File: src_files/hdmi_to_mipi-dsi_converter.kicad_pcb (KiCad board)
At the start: 4 copper layers, 90 x 55 mm, 145 parts, among them J1 HDMI-019S, J2 HDMI-019S, J3 Conn_02x05_Odd_Even, J4 USB_B_Micro, J5 XF2M60151AH, J6 Conn_01x02, J7 XF2M60151AH, U1 MCP1700-1202E_SOT23, U2 AX1007E18A, U3 ME6211A33PG-N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

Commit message: updated all files and production files as well
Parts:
- added R28: 0R, Resistor_SMD:R_0603_1608Metric, F.Cu at (165.6, 60.6)
- FB1, FB4: footprint Barrel - Audio Connectors:BEADC2012X105N -> Inductor_SMD:L_0603_1608Metric
- FB2: footprint Inductor_SMD:L_0805_2012Metric -> Inductor_SMD:L_0603_1608Metric
- FB3: footprint Resistor_SMD:R_0603_1608Metric -> Inductor_SMD:L_0603_1608Metric
- U8: footprint Barrel - Audio Connectors:QFN40P180X180X55-12N -> SamacSys_Parts_2:QFN40P180X180X55-12N
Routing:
- net GND: track 192.5 -> 191.7 mm, vias 118 -> 117

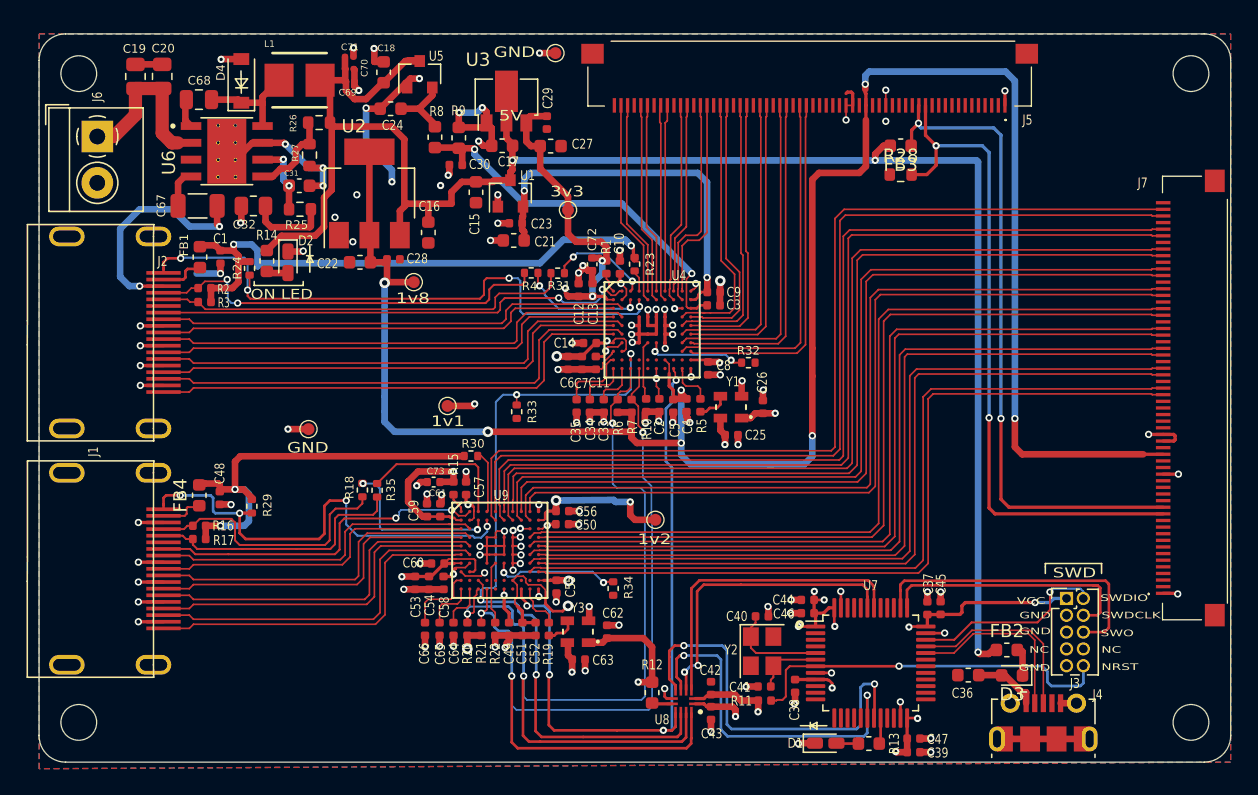
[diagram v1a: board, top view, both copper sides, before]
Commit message: reduced form factor
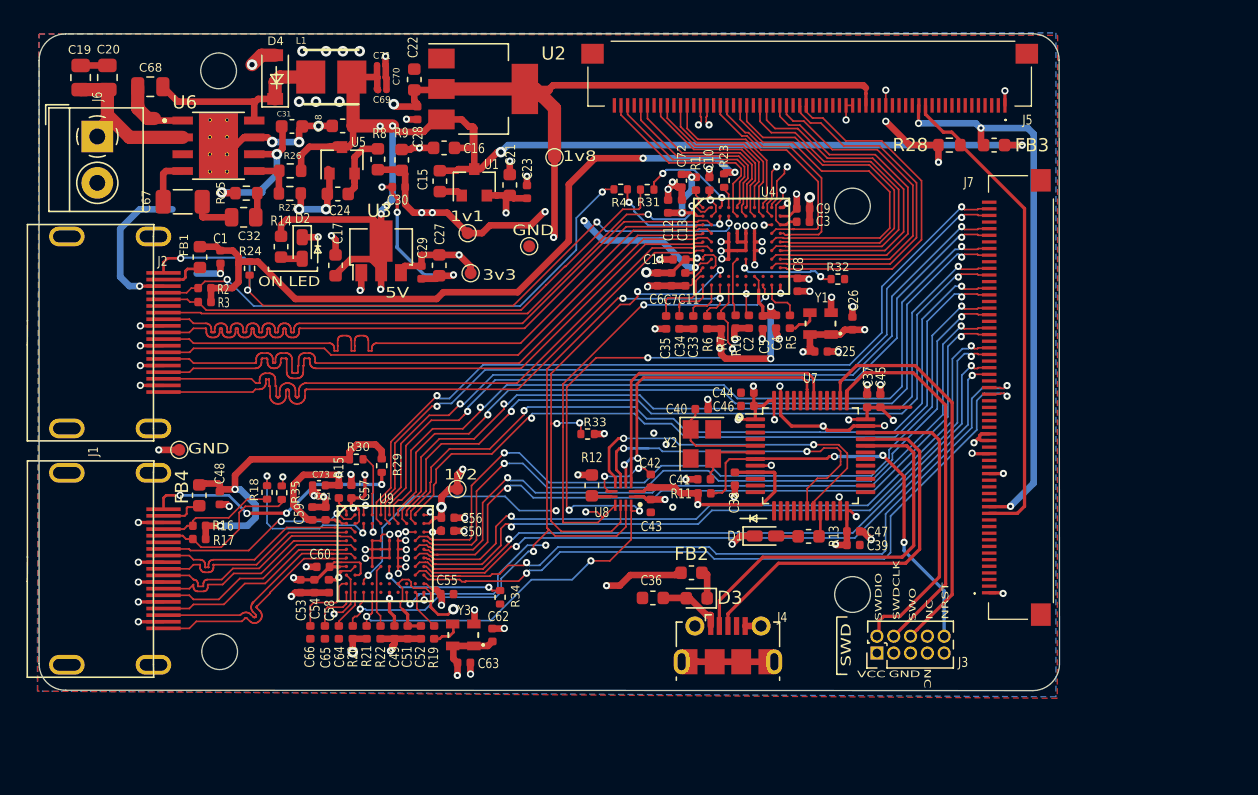
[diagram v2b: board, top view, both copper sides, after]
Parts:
- moved H3 27.5 mm to (161.9, 63.0)
- moved H4 27.3 mm to (161.9, 92.3)
- moved D3 24.5 mm to (150.2, 92.6)
- moved C36 24.5 mm to (146.9, 92.6)
- moved FB2 24.5 mm to (149.8, 90.7)
- moved J4 24.5 mm to (152.5, 96.2)
- moved C37 16.3 mm to (163.0, 77.7)
- moved C39 16.3 mm to (162.0, 88.6)
- moved C41 16.3 mm to (150.7, 83.6)
- moved C42 16.3 mm to (146.7, 83.8)
- moved C44 16.3 mm to (154.0, 77.1)
- moved C45 16.3 mm to (164.0, 77.7)
- moved C46 16.3 mm to (154.0, 78.1)
- moved C47 16.3 mm to (162.0, 87.6)
- moved R12 16.3 mm to (142.2, 84.1)
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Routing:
- net +1V8: track 228.3 -> 175.6 mm
- net /mcu_ctrl/DIFF_N: track 13.8 -> 29.2 mm
- net /mcu_ctrl/DIFF_P: track 14.3 -> 29.3 mm
- net /HDMIC_N: track 35.9 -> 50.7 mm
- net VSN: track 51.5 -> 36.7 mm, vias 2 -> 0
- net /HDMIC_P: track 35.1 -> 49.9 mm
- net +3V3: track 109.9 -> 124.3 mm, vias 23 -> 21
- net +5V: track 134.7 -> 148.3 mm, vias 3 -> 8
- net /HDMID0_N: track 36.6 -> 50.1 mm
- net /HDMID1_N: track 37.4 -> 50.2 mm
- net /HDMID1_P: track 36.7 -> 49.5 mm
- net /HDMID2_P: track 37.5 -> 49.8 mm
- net /HDMID2_N: track 38.2 -> 50.6 mm
- net /hdmi_mipi_2/CDSI1_TX_D3_P: track 72.1 -> 59.9 mm, vias 0 -> 2
- net /hdmi_mipi_2/CDSI1_TX_D3_N: track 73.4 -> 61.6 mm, vias 0 -> 2
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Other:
- board size 90 x 55 mm -> 77.1 x 49.6 mm

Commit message: update on HDMI to MIPI
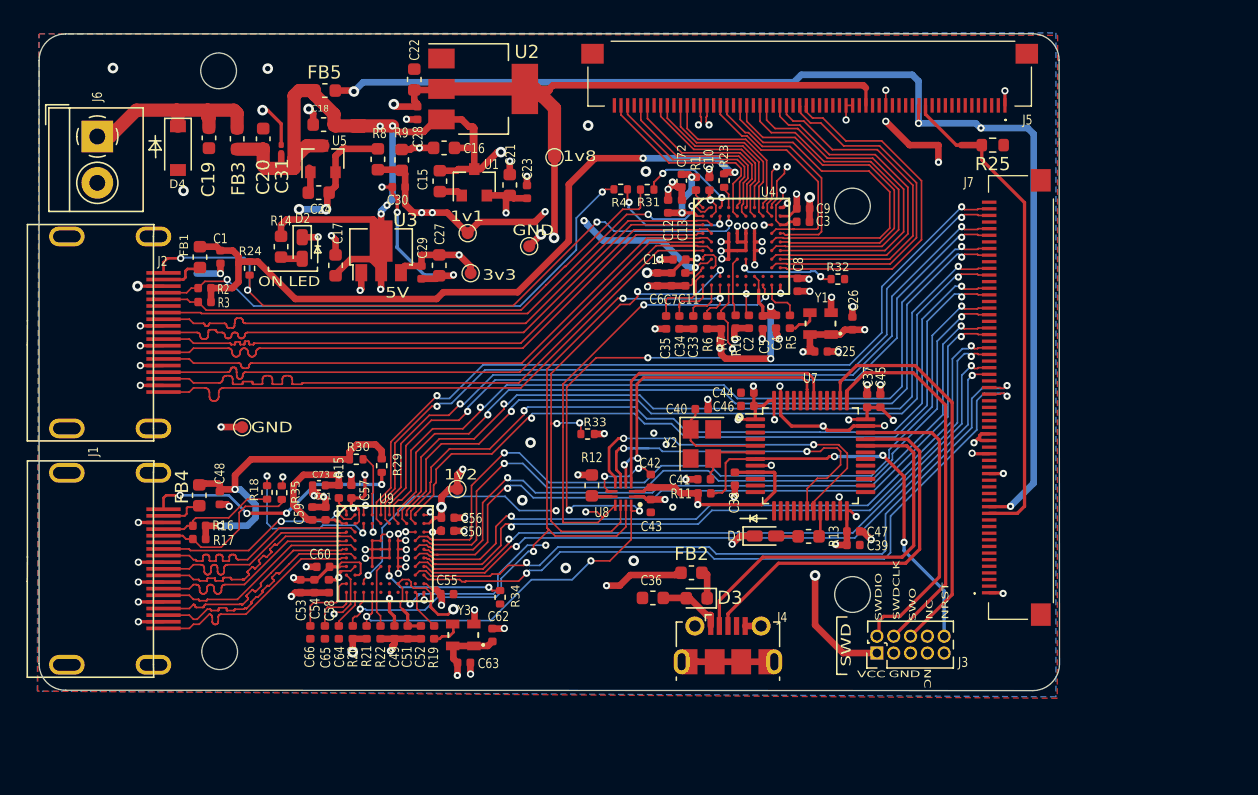
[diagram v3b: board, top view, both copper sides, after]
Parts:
- removed C32: 1.5nF, Resistor_SMD:R_0805_2012Metric
- removed C67: 8.2nF, Capacitor_SMD:C_1206_3216Metric
- removed C68: 100nF, Capacitor_SMD:C_0805_2012Metric
- removed C69, C70, C71: 22uF, Resistor_SMD:R_0201_0603Metric
- removed L1: 74438357068, 74438357068_ind:74438357068
- removed R26: 10.2k, Resistor_SMD:R_0603_1608Metric
- removed R27: 1.96k, Resistor_SMD:R_0603_1608Metric
- removed R28: 0R, Resistor_SMD:R_0603_1608Metric
- removed U6: TPS54332DDA, TPS54332:NOPB
- added FB5: FBMJ1608HS280NTR, Inductor_SMD:L_0603_1608Metric, F.Cu at (122.1, 54.3)
- C19: value 10uF -> 10u; footprint Resistor_SMD:R_0805_2012Metric -> Capacitor_SMD:C_0603_1608Metric
- C20: value 10uF -> 1uF; footprint Resistor_SMD:R_0805_2012Metric -> Capacitor_SMD:C_0603_1608Metric
- C31: value 10pF -> 22uF; footprint Capacitor_SMD:C_0603_1608Metric -> Resistor_SMD:R_0201_0603Metric
- R25: value 61.9K -> 0R
- moved FB3 57.2 mm to (115.5, 57.9), turned to 90 degrees
- moved R25 56.5 mm to (172.5, 58.4), turned to 180 degrees
- moved C20 12.6 mm to (117.4, 57.9)
- moved C19 10.7 mm to (113.3, 57.9), turned to 270 degrees
- moved D4 9.09 mm to (111.0, 58.6), turned to 270 degrees
- moved TP4 5.05 mm to (115.8, 79.7)
- moved C31 1.90 mm to (118.8, 58.7), turned to 90 degrees
- moved C18 1.44 mm to (122.0, 56.9)
- moved C24 1.44 mm to (121.6, 62.0)
- moved U5 1.44 mm to (121.9, 59.5)
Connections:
- C19 pad 1: /power/24VIN -> /power/5V_IN
- C20 pad 1: /power/24VIN -> +5V
- C31 pad 1: Net-(C31-Pad1) -> +5V
- D4 pad 1: Net-(C68-Pad2) -> /power/5V_IN
- FB3 pad 1: VSP -> +5V
- FB3 pad 2: +5V -> /power/5V_IN
- J6 pad 1: /power/24VIN -> /power/5V_IN
- R25 pad 1: Net-(C31-Pad1) -> GND
- R25 pad 2: Net-(C32-Pad2) -> VSN
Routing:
- net VSP: track 42.4 -> 89.0 mm, vias 3 -> 4
- net +5V: track 148.3 -> 114.9 mm, vias 8 -> 7
- net GND: track 202.9 -> 179.4 mm, vias 110 -> 108
- net /power/5V_IN: track 0.00 -> 15.5 mm
- net Net-(C68-Pad2): track 14.6 -> 0.00 mm
- net /power/24VIN: track 12.3 -> 0.00 mm
- net Net-(C31-Pad1): track 11.5 -> 0.00 mm, vias 2 -> 0
- net +3V3: track 124.3 -> 134.3 mm, vias 21 -> 22
- net Net-(C68-Pad1): track 5.92 -> 0.00 mm
- net Net-(C24-Pad1): track 5.16 -> 10.2 mm, vias 0 -> 2
- net /HDMIC_N: track 50.7 -> 46.1 mm
- net /HDMID1_N: track 50.2 -> 46.0 mm
- net /HDMID0_N: track 50.1 -> 46.0 mm
- net /HDMIC_P: track 49.9 -> 46.1 mm
- net Net-(C67-Pad1): track 3.68 -> 0.00 mm
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
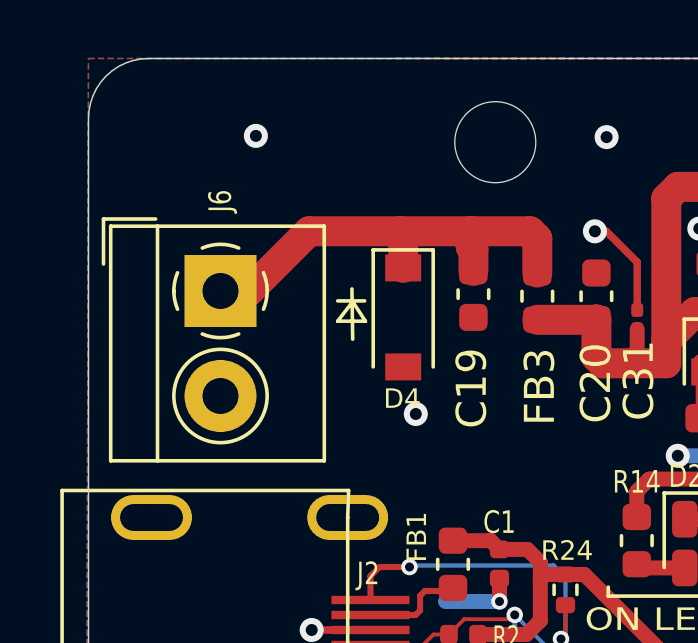
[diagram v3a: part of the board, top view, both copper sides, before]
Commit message: update on the hdmi to mipi
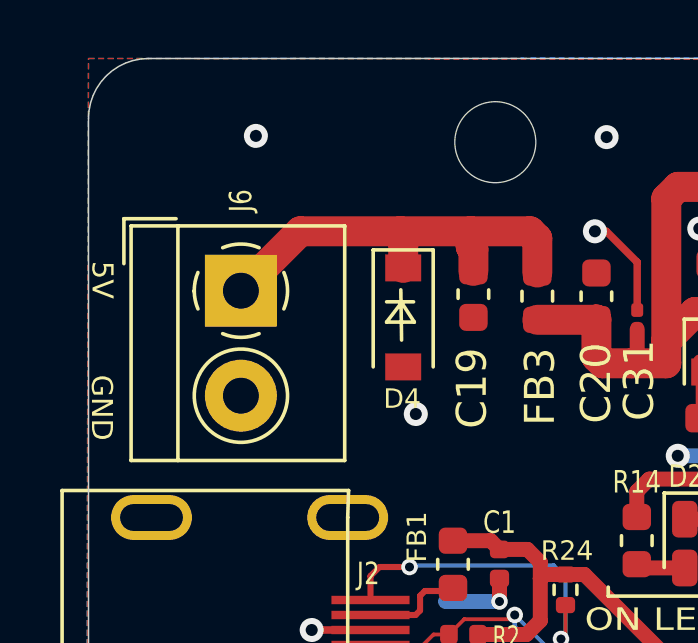
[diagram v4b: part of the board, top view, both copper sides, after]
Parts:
- moved J6 0.68 mm to (105.6, 57.7)
